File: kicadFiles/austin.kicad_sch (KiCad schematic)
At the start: 481 parts, among them J1 TYPE-C-31-M12_13, J5 ARM SWD, Q1 AO4406AL, Q2 DTC123J, SW1 MXSwitch, SW10 MXSwitch, SW100 MXSwitch, SW101 MXSwitch, SW102 MXSwitch, SW103 MXSwitch, SW104 MXSwitch, SW105 MXSwitch, SW106 MXSwitch, SW107 MXSwitch, SW108 MXSwitch, SW109 MXSwitch, SW11 MXSwitch, SW110 MXSwitch, SW111 MXSwitch, SW112 MXSwitch, SW113 MXSwitch, SW114 MXSwitch, SW12 MXSwitch, SW13 MXSwitch, SW14 MXSwitch, SW15 MXSwitch, SW16 MXSwitch, SW17 MXSwitch, SW18 MXSwitch, SW19 MXSwitch, SW2 MXSwitch, SW20 MXSwitch, SW21 MXSwitch, SW22 MXSwitch, SW23 MXSwitch, SW24 MXSwitch, SW25 MXSwitch, SW26 MXSwitch, SW27 MXSwitch, SW28 MXSwitch, SW29 MXSwitch, SW3 MXSwitch, SW30 MXSwitch, SW31 MXSwitch, SW32 MXSwitch, SW33 MXSwitch, SW34 MXSwitch, SW35 MXSwitch, SW36 MXSwitch, SW37 MXSwitch, SW38 MXSwitch, SW39 MXSwitch, SW4 MXSwitch, SW40 MXSwitch, SW41 MXSwitch, SW42 MXSwitch, SW43 MXSwitch, SW44 MXSwitch, SW45 MXSwitch, SW46 MXSwitch, SW47 MXSwitch, SW48 MXSwitch, SW49 MXSwitch, SW5 MXSwitch, SW50 MXSwitch, SW51 MXSwitch, SW52 MXSwitch, SW53 MXSwitch, SW54 MXSwitch, SW55 MXSwitch, SW56 MXSwitch, SW57 MXSwitch, SW58 ANSI LShift, SW59 MXSwitch, SW6 MXSwitch, SW60 MXSwitch, SW61 MXSwitch, SW62 MXSwitch, SW63 MXSwitch, SW64 MXSwitch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

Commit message: RGB placemente and routing, new MCU placement, rows traces patterns done
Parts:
- removed CB2, CB3, CB4: 100n, Capacitor_SMD:C_0805_2012Metric_Pad1.15x1.40mm_HandSolder, symbol Device:C_Small
- removed CB5: 10u, Capacitor_SMD:C_0805_2012Metric_Pad1.15x1.40mm_HandSolder, symbol Device:C_Small
- removed Q1: AO4406AL, acheronComponents:SOIC-8, symbol austin-rescue:AO4406AL-acheronSymbols-austin-rescue-austin-rescue
- removed RGP1: 10k, acheronComponents:R_SMD_1206, symbol Device:R_Small
- removed RGS1: 100, acheronComponents:R_SMD_1206, symbol Device:R_Small
- added C1, C11, C7: 1u, Capacitor_SMD:C_0805_2012Metric_Pad1.15x1.40mm_HandSolder, symbol Device:C_Small
- added C10, C5, C6: 100n, Capacitor_SMD:C_0805_2012Metric_Pad1.15x1.40mm_HandSolder, symbol Device:C_Small
- added C14, C15, C16, C17, C18, C19, C20, C21, C22, C23, C24, C25, C26, C27, C28, C29, C30, C31, C32, C33, C34, C35: 100n, Capacitor_SMD:C_0805_2012Metric, symbol Device:C
- added C8: 4.7u, Capacitor_SMD:C_0805_2012Metric_Pad1.15x1.40mm_HandSolder, symbol Device:C_Small
- added C9: 10n, Capacitor_SMD:C_0805_2012Metric_Pad1.15x1.40mm_HandSolder, symbol Device:C_Small
- added D109, D110, D111, D112, D113, D114, D115, D116, D117, D118, D119, D120, D121, D122, D123, D124, D125, D126, D127, D128: WS2812C, acheronComponents:LED_WS2812B_5.0x5.0mm_P3.2mm, symbol LED:WS2812B
- added Q1: AO3401A, Package_TO_SOT_SMD:SOT-23, symbol Transistor_FET:AO3401A
- added Q2: DTC123JKAT146, Package_TO_SOT_SMD:SOT-23, symbol acheronSymbols:DTC123J
- added R1: 1k, Resistor_SMD:R_0805_2012Metric, symbol Device:R
- added R119: 10k, Resistor_SMD:R_0805_2012Metric, symbol Device:R
- added R120, R121, R122, R123, R124, R125, R126, R127, R128, R129, R130, R131, R132, R133, R134, R135, R136, R137, R138, R139: 5R, Resistor_SMD:R_0805_2012Metric, symbol Device:R
- added R2: 100R, Resistor_SMD:R_0805_2012Metric, symbol Device:R
- added U4: TXS0101, acheronComponents:SOT-23-6, symbol acheronSymbols:TXS0101
- R10: renamed from RL8; value 360 -> 420; footprint acheronComponents:R_SMD_1206 -> Resistor_SMD:R_0805_2012Metric; Package (none) -> R0805
- R100: renamed from RL100; value 360 -> 420; footprint acheronComponents:R_SMD_1206 -> Resistor_SMD:R_0805_2012Metric; Package (none) -> R0805
- R101: renamed from RL101; value 360 -> 420; footprint acheronComponents:R_SMD_1206 -> Resistor_SMD:R_0805_2012Metric; Package (none) -> R0805
- R102: renamed from RL102; value 360 -> 420; footprint acheronComponents:R_SMD_1206 -> Resistor_SMD:R_0805_2012Metric; Package (none) -> R0805
- R103: renamed from RL103; value 360 -> 420; footprint acheronComponents:R_SMD_1206 -> Resistor_SMD:R_0805_2012Metric; Package (none) -> R0805
- R104: renamed from RL104; value 360 -> 420; footprint acheronComponents:R_SMD_1206 -> Resistor_SMD:R_0805_2012Metric; Package (none) -> R0805
- R105: renamed from RL105; value 360 -> 420; footprint acheronComponents:R_SMD_1206 -> Resistor_SMD:R_0805_2012Metric; Package (none) -> R0805
- R106: renamed from RL106; value 360 -> 420; footprint acheronComponents:R_SMD_1206 -> Resistor_SMD:R_0805_2012Metric; Package (none) -> R0805
- R107: renamed from RL107; value 360 -> 420; footprint acheronComponents:R_SMD_1206 -> Resistor_SMD:R_0805_2012Metric; Package (none) -> R0805
- R108: renamed from RL108; value 360 -> 420; footprint acheronComponents:R_SMD_1206 -> Resistor_SMD:R_0805_2012Metric; Package (none) -> R0805
- R11: renamed from RL9; value 360 -> 420; footprint acheronComponents:R_SMD_1206 -> Resistor_SMD:R_0805_2012Metric; Package (none) -> R0805
- R113: renamed from R7; value 360 -> 420
- R114: renamed from R8; value 360 -> 420
- R115: renamed from R9; value 360 -> 420
- R12: renamed from RL10; value 360 -> 420; footprint acheronComponents:R_SMD_1206 -> Resistor_SMD:R_0805_2012Metric; Package (none) -> R0805
- R13: renamed from RL11; value 360 -> 420; footprint acheronComponents:R_SMD_1206 -> Resistor_SMD:R_0805_2012Metric; Package (none) -> R0805
- R14: renamed from RL12; value 360 -> 420; footprint acheronComponents:R_SMD_1206 -> Resistor_SMD:R_0805_2012Metric; Package (none) -> R0805
- R15: renamed from RL13; value 360 -> 420; footprint acheronComponents:R_SMD_1206 -> Resistor_SMD:R_0805_2012Metric; Package (none) -> R0805
- R16: renamed from RL14; value 360 -> 420; footprint acheronComponents:R_SMD_1206 -> Resistor_SMD:R_0805_2012Metric; Package (none) -> R0805
- R17: renamed from RL15; value 360 -> 420; footprint acheronComponents:R_SMD_1206 -> Resistor_SMD:R_0805_2012Metric; Package (none) -> R0805
- R18: renamed from RL16; value 360 -> 420; footprint acheronComponents:R_SMD_1206 -> Resistor_SMD:R_0805_2012Metric; Package (none) -> R0805
- R19: renamed from RL17; value 360 -> 420; footprint acheronComponents:R_SMD_1206 -> Resistor_SMD:R_0805_2012Metric; Package (none) -> R0805
- R20: renamed from RL18; value 360 -> 420; footprint acheronComponents:R_SMD_1206 -> Resistor_SMD:R_0805_2012Metric; Package (none) -> R0805
- R21: renamed from RL19; value 360 -> 420; footprint acheronComponents:R_SMD_1206 -> Resistor_SMD:R_0805_2012Metric; Package (none) -> R0805
- R22: renamed from RL20; value 360 -> 420; footprint acheronComponents:R_SMD_1206 -> Resistor_SMD:R_0805_2012Metric; Package (none) -> R0805
- R23: renamed from RL21; value 360 -> 420; footprint acheronComponents:R_SMD_1206 -> Resistor_SMD:R_0805_2012Metric; Package (none) -> R0805
- R24: renamed from RL22; value 360 -> 420; footprint acheronComponents:R_SMD_1206 -> Resistor_SMD:R_0805_2012Metric; Package (none) -> R0805
- R25: renamed from RL23; value 360 -> 420; footprint acheronComponents:R_SMD_1206 -> Resistor_SMD:R_0805_2012Metric; Package (none) -> R0805
- R26: renamed from RL24; value 360 -> 420; footprint acheronComponents:R_SMD_1206 -> Resistor_SMD:R_0805_2012Metric; Package (none) -> R0805
- R27: renamed from RL25; value 360 -> 420; footprint acheronComponents:R_SMD_1206 -> Resistor_SMD:R_0805_2012Metric; Package (none) -> R0805
- R28: renamed from RL26; value 360 -> 420; footprint acheronComponents:R_SMD_1206 -> Resistor_SMD:R_0805_2012Metric; Package (none) -> R0805
- R29: renamed from RL27; value 360 -> 420; footprint acheronComponents:R_SMD_1206 -> Resistor_SMD:R_0805_2012Metric; Package (none) -> R0805
- R3: renamed from RL1; value 360 -> 420; footprint acheronComponents:R_SMD_1206 -> Resistor_SMD:R_0805_2012Metric; Package (none) -> R0805
- R30: renamed from RL28; value 360 -> 420; footprint acheronComponents:R_SMD_1206 -> Resistor_SMD:R_0805_2012Metric; Package (none) -> R0805
- R31: renamed from RL29; value 360 -> 420; footprint acheronComponents:R_SMD_1206 -> Resistor_SMD:R_0805_2012Metric; Package (none) -> R0805
- R32: renamed from RL30; value 360 -> 420; footprint acheronComponents:R_SMD_1206 -> Resistor_SMD:R_0805_2012Metric; Package (none) -> R0805
- R33: renamed from RL31; value 360 -> 420; footprint acheronComponents:R_SMD_1206 -> Resistor_SMD:R_0805_2012Metric; Package (none) -> R0805
- R34: renamed from RL32; value 360 -> 420; footprint acheronComponents:R_SMD_1206 -> Resistor_SMD:R_0805_2012Metric; Package (none) -> R0805
- R35: renamed from RL33; value 360 -> 420; footprint acheronComponents:R_SMD_1206 -> Resistor_SMD:R_0805_2012Metric; Package (none) -> R0805
- R36: renamed from RL34; value 360 -> 420; footprint acheronComponents:R_SMD_1206 -> Resistor_SMD:R_0805_2012Metric; Package (none) -> R0805
- R37: renamed from RL36; value 360 -> 420; footprint acheronComponents:R_SMD_1206 -> Resistor_SMD:R_0805_2012Metric; Package (none) -> R0805
- R38: renamed from RL37; value 360 -> 420; footprint acheronComponents:R_SMD_1206 -> Resistor_SMD:R_0805_2012Metric; Package (none) -> R0805
- R39: renamed from RL38; value 360 -> 420; footprint acheronComponents:R_SMD_1206 -> Resistor_SMD:R_0805_2012Metric; Package (none) -> R0805
- R4: renamed from RL2; value 360 -> 420; footprint acheronComponents:R_SMD_1206 -> Resistor_SMD:R_0805_2012Metric; Package (none) -> R0805
- R40: renamed from RL39; value 360 -> 420; footprint acheronComponents:R_SMD_1206 -> Resistor_SMD:R_0805_2012Metric; Package (none) -> R0805
- R41: renamed from RL40; value 360 -> 420; footprint acheronComponents:R_SMD_1206 -> Resistor_SMD:R_0805_2012Metric; Package (none) -> R0805
- R42: renamed from RL41; value 360 -> 420; footprint acheronComponents:R_SMD_1206 -> Resistor_SMD:R_0805_2012Metric; Package (none) -> R0805
- R43: renamed from RL42; value 360 -> 420; footprint acheronComponents:R_SMD_1206 -> Resistor_SMD:R_0805_2012Metric; Package (none) -> R0805
- R44: renamed from RL43; value 360 -> 420; footprint acheronComponents:R_SMD_1206 -> Resistor_SMD:R_0805_2012Metric; Package (none) -> R0805
- R45: renamed from RL44; value 360 -> 420; footprint acheronComponents:R_SMD_1206 -> Resistor_SMD:R_0805_2012Metric; Package (none) -> R0805
- R46: renamed from RL45; value 360 -> 420; footprint acheronComponents:R_SMD_1206 -> Resistor_SMD:R_0805_2012Metric; Package (none) -> R0805
- R47: renamed from RL46; value 360 -> 420; footprint acheronComponents:R_SMD_1206 -> Resistor_SMD:R_0805_2012Metric; Package (none) -> R0805
- R48: renamed from RL47; value 360 -> 420; footprint acheronComponents:R_SMD_1206 -> Resistor_SMD:R_0805_2012Metric; Package (none) -> R0805
- R49: renamed from RL48; value 360 -> 420; footprint acheronComponents:R_SMD_1206 -> Resistor_SMD:R_0805_2012Metric; Package (none) -> R0805
- R5: renamed from RL3; value 360 -> 420; footprint acheronComponents:R_SMD_1206 -> Resistor_SMD:R_0805_2012Metric; Package (none) -> R0805
- R50: renamed from RL49; value 360 -> 420; footprint acheronComponents:R_SMD_1206 -> Resistor_SMD:R_0805_2012Metric; Package (none) -> R0805
- R51: renamed from RL50; value 360 -> 420; footprint acheronComponents:R_SMD_1206 -> Resistor_SMD:R_0805_2012Metric; Package (none) -> R0805
- R52: renamed from RL51; value 360 -> 420; footprint acheronComponents:R_SMD_1206 -> Resistor_SMD:R_0805_2012Metric; Package (none) -> R0805
- R53: renamed from RL52; value 360 -> 420; footprint acheronComponents:R_SMD_1206 -> Resistor_SMD:R_0805_2012Metric; Package (none) -> R0805
- R54: renamed from RL53; value 360 -> 420; footprint acheronComponents:R_SMD_1206 -> Resistor_SMD:R_0805_2012Metric; Package (none) -> R0805
- R55: renamed from RL54; value 360 -> 420; footprint acheronComponents:R_SMD_1206 -> Resistor_SMD:R_0805_2012Metric; Package (none) -> R0805
- R56: renamed from RL55; value 360 -> 420; footprint acheronComponents:R_SMD_1206 -> Resistor_SMD:R_0805_2012Metric; Package (none) -> R0805
- R57: renamed from RL56; value 360 -> 420; footprint acheronComponents:R_SMD_1206 -> Resistor_SMD:R_0805_2012Metric; Package (none) -> R0805
- R58: renamed from RL57; value 360 -> 420; footprint acheronComponents:R_SMD_1206 -> Resistor_SMD:R_0805_2012Metric; Package (none) -> R0805
- R59: renamed from RL58; value 360 -> 420; footprint acheronComponents:R_SMD_1206 -> Resistor_SMD:R_0805_2012Metric; Package (none) -> R0805
- R6: renamed from RL4; value 360 -> 420; footprint acheronComponents:R_SMD_1206 -> Resistor_SMD:R_0805_2012Metric; Package (none) -> R0805
- R60: renamed from RL60; value 360 -> 420; footprint acheronComponents:R_SMD_1206 -> Resistor_SMD:R_0805_2012Metric; Package (none) -> R0805
- R61: renamed from RL62; value 360 -> 420; footprint acheronComponents:R_SMD_1206 -> Resistor_SMD:R_0805_2012Metric; Package (none) -> R0805
- R62: renamed from RL63; value 360 -> 420; footprint acheronComponents:R_SMD_1206 -> Resistor_SMD:R_0805_2012Metric; Package (none) -> R0805
- R63: renamed from RL64; value 360 -> 420; footprint acheronComponents:R_SMD_1206 -> Resistor_SMD:R_0805_2012Metric; Package (none) -> R0805
- R64: renamed from RL65; value 360 -> 420; footprint acheronComponents:R_SMD_1206 -> Resistor_SMD:R_0805_2012Metric; Package (none) -> R0805
- R65: renamed from RL66; value 360 -> 420; footprint acheronComponents:R_SMD_1206 -> Resistor_SMD:R_0805_2012Metric; Package (none) -> R0805
- R66: renamed from RL67; value 360 -> 420; footprint acheronComponents:R_SMD_1206 -> Resistor_SMD:R_0805_2012Metric; Package (none) -> R0805
- R67: renamed from RL68; value 360 -> 420; footprint acheronComponents:R_SMD_1206 -> Resistor_SMD:R_0805_2012Metric; Package (none) -> R0805
- R68: renamed from RL69; value 360 -> 420; footprint acheronComponents:R_SMD_1206 -> Resistor_SMD:R_0805_2012Metric; Package (none) -> R0805
- R69: renamed from RL70; value 360 -> 420; footprint acheronComponents:R_SMD_1206 -> Resistor_SMD:R_0805_2012Metric; Package (none) -> R0805
- R7: renamed from RL5; value 360 -> 420; footprint acheronComponents:R_SMD_1206 -> Resistor_SMD:R_0805_2012Metric; Package (none) -> R0805
- R70: renamed from RL71; value 360 -> 420; footprint acheronComponents:R_SMD_1206 -> Resistor_SMD:R_0805_2012Metric; Package (none) -> R0805
- R71: renamed from RL72; value 360 -> 420; footprint acheronComponents:R_SMD_1206 -> Resistor_SMD:R_0805_2012Metric; Package (none) -> R0805
- R72: renamed from RL73; value 360 -> 420; footprint acheronComponents:R_SMD_1206 -> Resistor_SMD:R_0805_2012Metric; Package (none) -> R0805
- R73: renamed from RL74; value 360 -> 420; footprint acheronComponents:R_SMD_1206 -> Resistor_SMD:R_0805_2012Metric; Package (none) -> R0805
- R74: renamed from RL75; value 360 -> 420; footprint acheronComponents:R_SMD_1206 -> Resistor_SMD:R_0805_2012Metric; Package (none) -> R0805
- R75: renamed from RL76; value 360 -> 420; footprint acheronComponents:R_SMD_1206 -> Resistor_SMD:R_0805_2012Metric; Package (none) -> R0805
- R76: renamed from RL77; value 360 -> 420; footprint acheronComponents:R_SMD_1206 -> Resistor_SMD:R_0805_2012Metric; Package (none) -> R0805
- R77: renamed from RL78; value 360 -> 420; footprint acheronComponents:R_SMD_1206 -> Resistor_SMD:R_0805_2012Metric; Package (none) -> R0805
- R78: renamed from RL79; value 360 -> 420; footprint acheronComponents:R_SMD_1206 -> Resistor_SMD:R_0805_2012Metric; Package (none) -> R0805
- R79: renamed from RL80; value 360 -> 420; footprint acheronComponents:R_SMD_1206 -> Resistor_SMD:R_0805_2012Metric; Package (none) -> R0805
- R8: renamed from RL6; value 360 -> 420; footprint acheronComponents:R_SMD_1206 -> Resistor_SMD:R_0805_2012Metric; Package (none) -> R0805
- R80: renamed from RL81; value 360 -> 420; footprint acheronComponents:R_SMD_1206 -> Resistor_SMD:R_0805_2012Metric; Package (none) -> R0805
- R81: renamed from RL82; value 360 -> 420; footprint acheronComponents:R_SMD_1206 -> Resistor_SMD:R_0805_2012Metric; Package (none) -> R0805
- R82: renamed from RL83; value 360 -> 420; footprint acheronComponents:R_SMD_1206 -> Resistor_SMD:R_0805_2012Metric; Package (none) -> R0805
- R83: renamed from RL84; value 360 -> 420; footprint acheronComponents:R_SMD_1206 -> Resistor_SMD:R_0805_2012Metric; Package (none) -> R0805
- R84: renamed from RL85; value 360 -> 420; footprint acheronComponents:R_SMD_1206 -> Resistor_SMD:R_0805_2012Metric; Package (none) -> R0805
- R85: renamed from RL86; value 360 -> 420; footprint acheronComponents:R_SMD_1206 -> Resistor_SMD:R_0805_2012Metric; Package (none) -> R0805
- R86: renamed from RL87; value 360 -> 420; footprint acheronComponents:R_SMD_1206 -> Resistor_SMD:R_0805_2012Metric; Package (none) -> R0805
- R87: renamed from RL88; value 360 -> 420; footprint acheronComponents:R_SMD_1206 -> Resistor_SMD:R_0805_2012Metric; Package (none) -> R0805
- R88: renamed from RL89; value 360 -> 420; footprint acheronComponents:R_SMD_1206 -> Resistor_SMD:R_0805_2012Metric; Package (none) -> R0805
- R89: renamed from RL90; value 360 -> 420; footprint acheronComponents:R_SMD_1206 -> Resistor_SMD:R_0805_2012Metric; Package (none) -> R0805
- R9: renamed from RL7; value 360 -> 420; footprint acheronComponents:R_SMD_1206 -> Resistor_SMD:R_0805_2012Metric; Package (none) -> R0805
- R90: renamed from RL91; value 360 -> 420; footprint acheronComponents:R_SMD_1206 -> Resistor_SMD:R_0805_2012Metric; Package (none) -> R0805
- R91: renamed from RL35; value 360 -> 420; footprint acheronComponents:R_SMD_1206 -> Resistor_SMD:R_0805_2012Metric; Package (none) -> R0805
- R92: renamed from RL92; value 360 -> 420; footprint acheronComponents:R_SMD_1206 -> Resistor_SMD:R_0805_2012Metric; Package (none) -> R0805
- R93: renamed from RL93; value 360 -> 420; footprint acheronComponents:R_SMD_1206 -> Resistor_SMD:R_0805_2012Metric; Package (none) -> R0805
- R94: renamed from RL94; value 360 -> 420; footprint acheronComponents:R_SMD_1206 -> Resistor_SMD:R_0805_2012Metric; Package (none) -> R0805
- R95: renamed from RL95; value 360 -> 420; footprint acheronComponents:R_SMD_1206 -> Resistor_SMD:R_0805_2012Metric; Package (none) -> R0805
- R96: renamed from RL96; value 360 -> 420; footprint acheronComponents:R_SMD_1206 -> Resistor_SMD:R_0805_2012Metric; Package (none) -> R0805
- R97: renamed from RL97; value 360 -> 420; footprint acheronComponents:R_SMD_1206 -> Resistor_SMD:R_0805_2012Metric; Package (none) -> R0805
- R98: renamed from RL98; value 360 -> 420; footprint acheronComponents:R_SMD_1206 -> Resistor_SMD:R_0805_2012Metric; Package (none) -> R0805
- R99: renamed from RL99; value 360 -> 420; footprint acheronComponents:R_SMD_1206 -> Resistor_SMD:R_0805_2012Metric; Package (none) -> R0805
- U2: renamed from U1; value STM32F072_LQFP48 -> STM32F072CBT6; symbol austin-rescue:STM32F072_LQFP48-acheronSymbols-austin-rescue-austin-rescue -> acheronSymbols:STM32F072-LQFP48; LCSC Part Number (none) -> C81720; Manufacturer (none) -> STMicroelectronics; Manufacturer Part Number (none) -> STM32F072CBT6; Package (none) -> LQFP-48
- renumbered C3 to C12, C4 to C13, CB1 to C2, C1 to C3, C2 to C4, D103 to D100, D105 to D101, D106 to D102, D107 to D103, D108 to D104, D104 to D105, D58 to D106, D78 to D107, D60 to D108, D35 to D34, D36 to D35, D37 to D36, D38 to D37, D39 to D38, D40 to D39, D41 to D40, D42 to D41, D43 to D42, D44 to D43, D45 to D44, D46 to D45, D47 to D46, D48 to D47, D49 to D48, D50 to D49, D51 to D50, D52 to D51, D53 to D52, D54 to D53, D55 to D54, D56 to D55, D57 to D56, D61 to D57, D62 to D58, D63 to D59, D64 to D60, D65 to D61, D66 to D62, D67 to D63, D68 to D64, D69 to D65, D70 to D66, D71 to D67, D72 to D68, D73 to D69, D74 to D70, D75 to D71, D76 to D72, D77 to D73, D59 to D74, D90 to D75, D79 to D76, D34 to D77, D80 to D78, D81 to D79, D82 to D80, D83 to D81, D84 to D82, D85 to D83, D86 to D84, D87 to D85, D88 to D86, D89 to D87, D91 to D88, D92 to D89, D93 to D90, D94 to D91, D95 to D92, D96 to D93, D97 to D94, D98 to D95, D99 to D96, D100 to D97, D101 to D98, D102 to D99, J5 to J1, J1 to J2, LED109 to LED100, LED110 to LED101, LED97 to LED102, LED98 to LED103, LED99 to LED104, LED111 to LED105, LED100 to LED106, LED101 to LED107, LED102 to LED108, LED103 to LED109, LED104 to LED110, LED112 to LED111, LED105 to LED112, LED106 to LED113, LED107 to LED114, LED108 to LED115, LED35 to LED34, LED34 to LED35, LED114 to LED54, LED54 to LED55, LED55 to LED56, LED56 to LED57, LED57 to LED58, LED58 to LED59, LED61 to LED60, LED60 to LED61, LED115 to LED73, LED73 to LED74, LED74 to LED75, LED75 to LED76, LED76 to LED77, LED77 to LED78, LED78 to LED79, LED59 to LED80, LED79 to LED81, LED80 to LED82, LED81 to LED83, LED82 to LED84, LED83 to LED85, LED84 to LED86, LED85 to LED87, LED86 to LED88, LED87 to LED89, LED88 to LED90, LED89 to LED91, LED90 to LED92, LED91 to LED93, LED96 to LED94, LED92 to LED95, LED93 to LED96, LED94 to LED97, LED95 to LED98, LED113 to LED99, LEDSCRL1 to LEDSCR1, Q2 to Q3, R1 to R109, R10 to R110, R2 to R111, R3 to R112, R4 to R116, R5 to R117, R6 to R118, SW99 to SW100, SW100 to SW101, SW101 to SW102, SW102 to SW103, SW103 to SW104, SW98 to SW111, SW111 to SW112, SW104 to SW113, SW112 to SW114, SW35 to SW34, SW36 to SW35, SW37 to SW36, SW38 to SW37, SW39 to SW38, SW34 to SW39, SW113 to SW40, SW40 to SW41, SW41 to SW42, SW42 to SW43, SW43 to SW44, SW44 to SW45, SW45 to SW46, SW46 to SW47, SW47 to SW48, SW48 to SW49, SW49 to SW50, SW50 to SW51, SW51 to SW52, SW52 to SW53, SW53 to SW54, SW54 to SW55, SW55 to SW56, SW56 to SW57, SW57 to SW58, SW114 to SW59, SW62 to SW61, SW63 to SW62, SW64 to SW63, SW65 to SW64, SW66 to SW65, SW67 to SW66, SW68 to SW67, SW69 to SW68, SW70 to SW69, SW71 to SW70, SW72 to SW71, SW73 to SW72, SW74 to SW73, SW75 to SW74, SW76 to SW75, SW77 to SW76, SW59 to SW77, SW61 to SW78, SW58 to SW79, SW90 to SW80, SW79 to SW81, SW78 to SW82, SW80 to SW83, SW81 to SW84, SW82 to SW85, SW83 to SW86, SW84 to SW87, SW85 to SW88, SW86 to SW89, SW87 to SW90, SW88 to SW91, SW89 to SW92, SW91 to SW93, SW92 to SW94, SW93 to SW95, SW94 to SW96, SW95 to SW97, SW96 to SW98, SW97 to SW99, U2 to U1
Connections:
- net 3.3V: now also C2.2, C1.2, C10.2, C11.2, C5.1, C6.2, C7.2, C8.2, C9.2; no longer C2.1
- net 5V: now also C15.1, Q1.2 (S), R1.1, R120.2, R121.2, R122.2, R123.2, R124.2, R125.2, R126.2, R127.2, R128.2, R129.2, R130.2, R131.2, R132.2, R133.2, R134.2, R135.2, R136.2, R137.2, R138.2, R139.2, U4.6 (VCCB); no longer R10.1, R100.1, R101.1, R102.1, R103.1, R104.1, R105.1, R106.1, R107.1, R108.1, R11.1, R12.1, R13.1, R14.1, R15.1, R16.1, R17.1, R18.1, R19.1, R20.1, R21.1, R22.1, R23.1, R24.1, R25.1, R26.1, R27.1, R28.1, R29.1, R3.1, R30.1, R31.1, R32.1, R33.1, R34.1, R35.1, R36.1, R37.1, R38.1, R39.1, R4.1, R40.1, R41.1, R42.1, R43.1, R44.1, R45.1, R46.1, R47.1, R48.1, R49.1, R5.1, R50.1, R51.1, R52.1, R53.1, R54.1, R55.1, R56.1, R57.1, R58.1, R59.1, R6.1, R60.1, R61.1, R62.1, R63.1, R64.1, R65.1, R66.1, R67.1, R68.1, R69.1, R7.1, R70.1, R71.1, R72.1, R73.1, R74.1, R75.1, R76.1, R77.1, R78.1, R79.1, R8.1, R80.1, R81.1, R82.1, R83.1, R84.1, R85.1, R86.1, R87.1, R88.1, R89.1, R9.1, R90.1, R91.1, R92.1, R93.1, R94.1, R95.1, R96.1, R97.1, R98.1, R99.1
- net Col1: now also SW1.2 (Row); no longer SW1.1 (Col), U2.21 (SPI2_CK/I2C2_SCL/TIM2_CH3/PB10)
- net Col10: now also SW10.2 (Row); no longer SW10.1 (Col), U2.15 (SPI1_SCK/I2S1_CK/ADCIN4/DACOUT1/PA5)
- net Col11: no longer U2.38 (PA15)
- net Col12: no longer U2.39 (SPI1_SCK/I2S1CK/PB3)
- net Col13: no longer U2.40 (SPI1_MISO_I2S1MCK/PB4)
- net Col14: no longer U2.41 (TIM3_CH2/SPI1_MOSI/I2S1_SD/I2C1_SMBA/PB5)
- net Col15: no longer U2.45 (I2C1SCL/PB8)
- net Col16: no longer U2.13 (TIM2_CH4/ADCIN3/PA3)
- net Col17: no longer U2.4 (PC15/Osc32Out)
- net Col18: no longer U2.3 (PC14/Osc32In)
- net Col19: no longer U2.6 (PF1/OscOut)
- net Col2: no longer U2.22 (I2C2_SDA/TIM2_CH4/EVENTOUT/PB11)
- net Col3: no longer U2.25 (EVENTOUT/PB12)
- net Col4: no longer U2.26 (SPI2_SCK/I2S2_CK/I2C2_SCL/PB13)
- net Col5: no longer U2.27 (SPI2_MISO/I2S2_MCK/I2C2_SDA/PB14)
- net Col6: now also SW6.2 (Row); no longer SW6.1 (Col), U2.28 (SPI2_MOSI/I2S2_SD/PB15)
- net Col7: no longer U2.29 (TIM1_CH1/EVENTOUT/MCO/PA8)
- net Col8: no longer U2.30 (TIM1_CH2/PA9)
- net Col9: no longer U2.31 (TIM1_CH3/PA10)
- net GND: now also C2.1, C1.1, C10.1, C11.1, C14.1, C15.2, C16.1, C17.1, C18.1, C19.1, C20.1, C21.1, C22.1, C23.1, C24.1, C25.1, C26.1, C27.1, C28.1, C29.1, C30.1, C31.1, C32.1, C33.1, C34.1, C35.1, C5.2, C6.1, C7.1, C8.1, C9.1, D109.3 (VSS), D110.3 (VSS), D111.3 (VSS), D112.3 (VSS), D113.3 (VSS), D114.3 (VSS), D115.3 (VSS), D116.3 (VSS), D117.3 (VSS), D118.3 (VSS), D119.3 (VSS), D120.3 (VSS), D121.3 (VSS), D122.3 (VSS), D123.3 (VSS), D124.3 (VSS), D125.3 (VSS), D126.3 (VSS), D127.3 (VSS), D128.3 (VSS), Q2.2 (E), U4.2 (GND); no longer C2.2
- net INDICATOR1: no longer U2.10 (ADCIN2/PA0)
- net INDICATOR2: no longer U2.12 (TIM2_CH3/ADCIN2/WKUP4/PA2)
- net INDICATOR3: no longer U2.11 (ADCIN1/PA1)
- net LED_PWM: now also Q2.1 (B)
- net Row1: no longer U2.2 (PC13/WKUP2)
- net Row2: no longer U2.14 (SPI1_NSS/I2S1_WS/ADCIN4/DACOUT2/PA4)
- net Row3: no longer U2.17 (SPI1_MOSI/I2S1_SD/TIM3_CH2/ADCIN7/PA7)
- net Row4: no longer U2.18 (TIM3_CH3/ADCIN8/PB0)
- net Row5: no longer U2.19 (TIM3_CH4/ADCIN9/PB1)
- net Row6: no longer U2.20 (PB2)
- net at D1.2 (A): now also SW1.1 (Col); no longer SW1.2 (Row)
- net at D6.2 (A): now also SW6.1 (Col); no longer SW6.2 (Row)
- net at D10.2 (A): now also SW10.1 (Col); no longer SW10.2 (Row)
- new net: Q1.3 (D), R10.1, R100.1, R101.1, R102.1, R103.1, R104.1, R105.1, R106.1, R107.1, R108.1, R11.1, R12.1, R13.1, R14.1, R15.1, R16.1, R17.1, R18.1, R19.1, R20.1, R21.1, R22.1, R23.1, R24.1, R25.1, R26.1, R27.1, R28.1, R29.1, R3.1, R30.1, R31.1, R32.1, R33.1, R34.1, R35.1, R36.1, R37.1, R38.1, R39.1, R4.1, R40.1, R41.1, R42.1, R43.1, R44.1, R45.1, R46.1, R47.1, R48.1, R49.1, R5.1, R50.1, R51.1, R52.1, R53.1, R54.1, R55.1, R56.1, R57.1, R58.1, R59.1, R6.1, R60.1, R61.1, R62.1, R63.1, R64.1, R65.1, R66.1, R67.1, R68.1, R69.1, R7.1, R70.1, R71.1, R72.1, R73.1, R74.1, R75.1, R76.1, R77.1, R78.1, R79.1, R8.1, R80.1, R81.1, R82.1, R83.1, R84.1, R85.1, R86.1, R87.1, R88.1, R89.1, R9.1, R90.1, R91.1, R92.1, R93.1, R94.1, R95.1, R96.1, R97.1, R98.1, R99.1
- new net: C33.2, D126.1 (VDD), R137.1
- new net: D126.2 (DOUT), D127.4 (DIN)
- new net: D125.2 (DOUT), D126.4 (DIN)
- new net: C28.2, D121.1 (VDD), R132.1
- new net: C23.2, D116.1 (VDD), R127.1
- new net: C27.2, D120.1 (VDD), R131.1
- new net: R119.1, U4.5 (OE)
- new net: C26.2, D119.1 (VDD), R130.1
- new net: C16.2, D109.1 (VDD), R120.1
- new net: C31.2, D124.1 (VDD), R135.1
- new net: C22.2, D115.1 (VDD), R126.1
- new net: Q2.3 (C), R1.2, R2.2
- new net: D116.2 (DOUT), D117.4 (DIN)
- new net: D115.2 (DOUT), D116.4 (DIN)
- new net: Q1.1 (G), R2.1
- new net: C32.2, D125.1 (VDD), R136.1
- new net: D124.2 (DOUT), D125.4 (DIN)
- new net: D119.2 (DOUT), D120.4 (DIN)
- new net: D118.2 (DOUT), D119.4 (DIN)
- new net: C24.2, D117.1 (VDD), R128.1
- new net: C19.2, D112.1 (VDD), R123.1
- new net: D114.2 (DOUT), D115.4 (DIN)
- new net: C25.2, D118.1 (VDD), R129.1
- new net: C29.2, D122.1 (VDD), R133.1
- new net: D121.2 (DOUT), D122.4 (DIN)
- new net: D120.2 (DOUT), D121.4 (DIN)
- new net: C21.2, D114.1 (VDD), R125.1
- new net: D113.2 (DOUT), D114.4 (DIN)
- new net: C30.2, D123.1 (VDD), R134.1
- new net: D123.2 (DOUT), D124.4 (DIN)
- new net: D122.2 (DOUT), D123.4 (DIN)
- new net: D109.2 (DOUT), D110.4 (DIN)
- new net: C35.2, D128.1 (VDD), R139.1
- new net: C20.2, D113.1 (VDD), R124.1
- new net: D117.2 (DOUT), D118.4 (DIN)
- new net: C17.2, D110.1 (VDD), R121.1
- new net: D110.2 (DOUT), D111.4 (DIN)
- new net: D112.2 (DOUT), D113.4 (DIN)
- new net: D111.2 (DOUT), D112.4 (DIN)
- new net: C34.2, D127.1 (VDD), R138.1
- new net: D127.2 (DOUT), D128.4 (DIN)
- new net: C18.2, D111.1 (VDD), R122.1
- new net 3V3: C14.2, R119.2, U4.1 (VCCA)
- new net RGB_3V3: U2.28 (SPI2_MOSI/I2S2_SD/PB15), U4.3 (A)
- new net RGB_5V: D109.4 (DIN), U4.4 (B)
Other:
- note removed: "Bypass capacitors"
- note removed: "CBs for "Capacitors - Bypass""
- note removed: "CRI for Capacitor - Regulator Input"
- note removed: "CRO for Capacitor - Regulator Output"
- note removed: "DF for "Diode - Fuse""
- note removed: "DS33 for "Schottky Diode - 3.3V""
- note removed: "RGP for "Gate Parallel" RGS for "Gate Series""
- moved on the sheet: C2, LED1, LED10, LED100, LED101, LED102, LED103, LED104, LED105, LED106, LED107, LED108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

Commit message: 3rd and 4th rows routing, hybrid dual package footprint for MCU
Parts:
- added R140: 420, Resistor_SMD:R_0805_2012Metric, symbol Device:R_Small
- U2: footprint acheronComponents:LQFP-48_7x7mm_P0.5mm -> acheronComponents:LQFP48_UFQFPN48_7x7mm_P0.5mm; symbol acheronSymbols:STM32F072-LQFP48 -> acheronSymbols:STM32F072-UFQFPN48; Manufacturer Part Number STM32F072CBT6 -> STM32F072CBU6; Package LQFP-48 -> UFQFPN-48
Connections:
- net 5V: now also LEDCAPS1.A, LEDNUM1.A, LEDSCR1.A
- net Col1: now also SW20.2 (Row); no longer SW20.1 (Col)
- net Col10: no longer SW101.1 (Col)
- net Col11: now also SW101.1 (Col); no longer SW102.1 (Col)
- net Col12: now also SW102.1 (Col); no longer SW103.1 (Col)
- net Col13: no longer SW104.1 (Col)
- net Col14: now also SW104.1 (Col), SW73.1 (Col)
- net Col15: now also SW74.1 (Col), SW94.1 (Col); no longer SW73.1 (Col)
- net Col16: now also SW75.1 (Col), SW95.1 (Col); no longer SW74.1 (Col), SW94.1 (Col)
- net Col17: now also SW76.1 (Col), SW96.1 (Col); no longer SW75.1 (Col), SW95.1 (Col)
- net Col18: now also SW77.1 (Col), SW97.1 (Col); no longer SW76.1 (Col), SW96.1 (Col)
- net Col19: no longer SW77.1 (Col), SW97.1 (Col)
- net Col2: now also SW42.2 (Row); no longer SW42.1 (Col)
- net GND: now also U2.49 (PAD); no longer LEDCAPS1.K, LEDNUM1.K, LEDSCR1.K
- net INDICATOR1: now also R113.2; no longer R113.1
- net Row3: now also D104.1 (K)
- net Row6: no longer D104.1 (K)
- net at Q1.3 (D), R10.1, R100.1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: now also R140.1
- net at D20.2 (A): now also SW20.1 (Col); no longer SW20.2 (Row)
- net at D40.2 (A): now also SW42.1 (Col); no longer SW42.2 (Row)
- net at LED72.A, R71.2: no longer LED73.A
- net at R114.2: now also LEDNUM1.K; no longer LEDNUM1.A
- net at R115.2: now also LEDCAPS1.K; no longer LEDCAPS1.A
- new net: LEDSCR1.K, R113.1
- new net: LED73.A, R140.2
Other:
- note added: "GRAVE"
- note removed: "`~"
- moved on the sheet: D100, D104, D70, D71, D72, D73, D74, D89, D90, D91, D92, D97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

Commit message: Routing finished. DRC and label pending
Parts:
- added J3: Conn_01x04, acheronConnectors:PinHeader_1x4_P2.54mm_Vertical, symbol Connector_Generic:Conn_01x04
- C1, C10, C11, C2, C5, C6, C7, C8: footprint Capacitor_SMD:C_0805_2012Metric_Pad1.15x1.40mm_HandSolder -> Capacitor_SMD:C_0402_1005Metric; Package (none) -> C0402
- C12, C13: footprint Capacitor_SMD:C_0805_2012Metric_Pad1.15x1.40mm_HandSolder -> Capacitor_SMD:C_0805_2012Metric
- C9: footprint Capacitor_SMD:C_0805_2012Metric_Pad1.15x1.40mm_HandSolder -> Capacitor_SMD:C_0402_1005Metric
- J1: footprint acheronConnectors:Conn_ARM_JTAG_SWD_6 -> acheronConnectors:Conn_ARM_JTAG_SWD_8; symbol Connector_Generic:Conn_02x03_Odd_Even -> Connector_Generic:Conn_02x04_Odd_Even
- R116, R117, R118: footprint acheronComponents:R_SMD_1206 -> Resistor_SMD:R_0805_2012Metric
- U2: LCSC Part Number C81720 -> C92504; Package UFQFPN-48 -> UFQFPN48
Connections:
- net 3.3V is gone; now on net 3V3: C1.2, C10.2, C11.2, C2.2, C4.1, C5.1, C6.2, C7.2, C8.2, C9.2, D106.2 (A), J1.1 (Pin_1), R110.1, S1.1, U1.2 (VO), U2.1 (VBAT), U2.24 (VDD), U2.36 (VDDIO2), U2.48 (VDD), U2.9 (VDDA)
- net nRST is gone; now on net NRST: J1.3 (Pin_3)
- net 3V3: now also J3.1 (Pin_1)
- net BOOT0: now also J1.8 (Pin_8)
- net Col1: now also U2.22 (PB11/TIM2_CH4/I2C2_SDA)
- net Col10: now also U2.4 (PC15/OSC32_OUT)
- net Col11: now also U2.3 (PC14/OSC32_IN)
- net Col12: now also U2.2 (PC13)
- net Col13: now also U2.21 (PB10/SPI2_SCK/I2C2_SCL/TIM2_CH3)
- net Col14: now also U2.20 (PB2)
- net Col15: now also U2.42 (I2C1_SCL/PB6)
- net Col16: now also U2.41 (SPI1_MOSI/I2S1_SD/TIM3_CH2/PB5)
- net Col17: now also U2.40 (SPI1_MISO/I2S1_MCK/TIM3_CH1/PB4)
- net Col18: now also U2.39 (SPI1_SCK/I2S1_CK/TIM2_CH2/PB3)
- net Col19: now also U2.38 (PA15)
- net Col2: now also U2.15 (PA5/ADC_IN5/DAC_OUT2)
- net Col3: now also U2.14 (PA4/TIM14_CH1/ADC_IN4)
- net Col4: now also U2.13 (PA3/TIM15_CH2/ADC_IN3)
- net Col5: now also U2.12 (PA2/ADC_IN2)
- net Col6: now also U2.11 (PA1/ADC_IN1)
- net Col7: now also U2.10 (PA0/ADC_IN0)
- net Col8: now also U2.6 (PF1/OSC_OUT)
- net Col9: now also U2.5 (PF0/OSC_IN)
- net GND: now also J1.7 (Pin_7), J3.4 (Pin_4)
- net INDICATOR1: now also U2.19 (PB1/TIM3_CH4/TIM14_CH1/ADC_IN9)
- net INDICATOR2: now also U2.17 (PA7/TIM3_CH2/TIM14_CH1/ADC_IN7)
- net INDICATOR3: now also U2.18 (PB0/TIM3_CH3/ADC_IN8)
- net Row1: now also U2.46 (SPI2_NSS/I2S2_WS/I2C1_SDA/TIM17_CH1/PB9)
- net Row2: now also U2.45 (I2C1_SCL/TIM16_CH1/PB8)
- net Row3: now also U2.43 (2C1_SDA/PB7)
- net Row4: now also U2.25 (PB12)
- net Row5: now also U2.27 (SPI2_MISO/I2S2_MCK/I2C2_SDA/TIM15_CH1/PB14)
- net Row6: now also U2.29 (TIM1_CH1/PA8)
- net EXTRA2: now reaches U2.30 (TIM1_CH2/PA9)
- net EXTRA2: now also J3.3 (Pin_3)
- net EXTRA1: now reaches U2.31 (TIM1_CH3/PA10)
- net EXTRA1: now also J3.2 (Pin_2)
- no-connect marks 2 -> 3

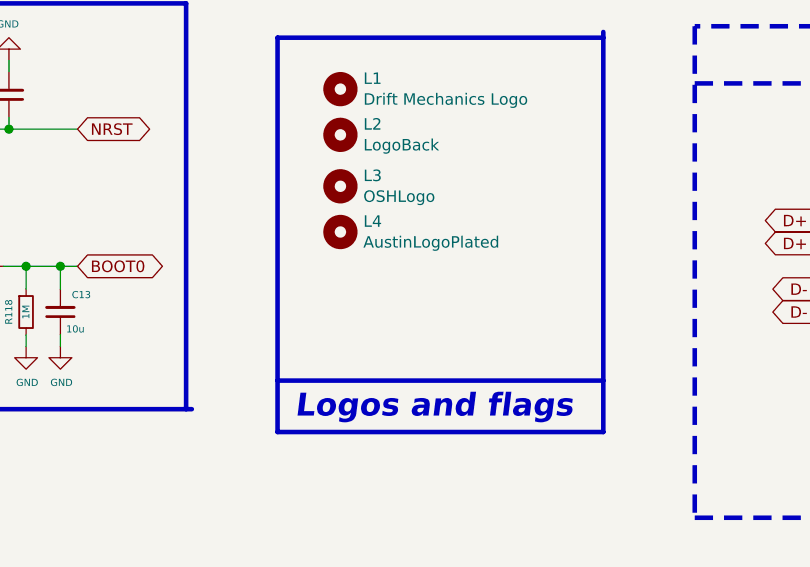
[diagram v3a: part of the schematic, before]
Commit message: Updated label, finish fab layers
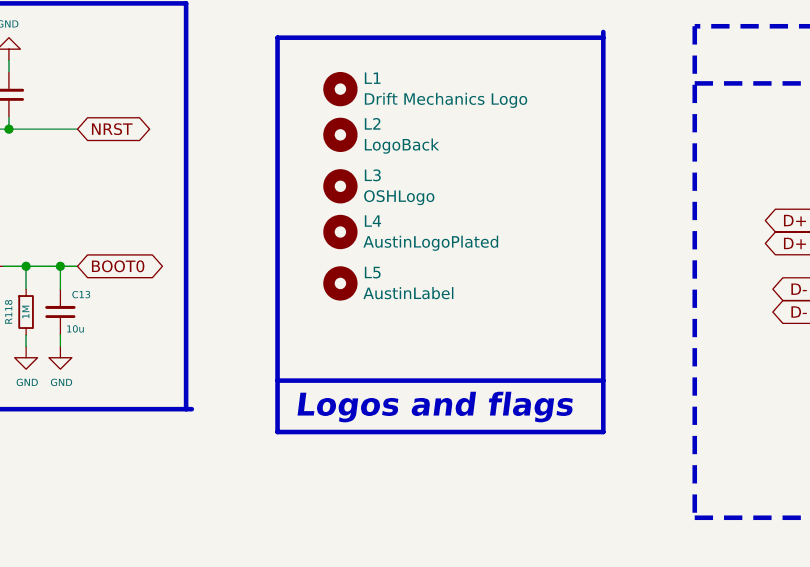
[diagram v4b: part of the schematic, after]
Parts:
- added L5: AustinLabel, austinLogo:austinLabel, symbol Mechanical:MountingHole
- L1, L2, L3, L4: now left out of the parts list
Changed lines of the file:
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@@
   (title_block
     (title "AustinPCB")
-    (date "2020-11-02")
-    (rev "v2.0.4")
+    (date "2020-11-03")
+    (rev "v2.0.5")
     (company "Designed by Gondolindrim")
     (comment 1 "In partnership with driftingbunnies and PheonixStar")
@@
   (junction (at 1123.95 515.62) (diameter 1.016) (color 0 0 0 0))
   (no_connect (at 234.315 304.165))
-  (no_connect (at 234.315 301.625))
   (no_connect (at 730.25 319.405))
+  (no_connect (at 234.315 301.625))
   (wire (pts (xy 44.45 35.56) (xy 66.04 35.56))
     (stroke (width 0) (type solid) (color 0 0 0 0))
@@
   )
   (symbol (lib_id "Mechanical:MountingHole") (at 266.7 364.49 0) (unit 1)
-    (in_bom yes) (on_board yes)
+    (in_bom no) (on_board yes)
     (property "Reference" "L1" (id 0) (at 269.24 363.3216 0)
       (effects (font (size 1.27 1.27)) (justify left))
@@
   )
   (symbol (lib_id "Mechanical:MountingHole") (at 266.7 369.57 0) (unit 1)
-    (in_bom yes) (on_board yes)
+    (in_bom no) (on_board yes)
     (property "Reference" "L2" (id 0) (at 269.24 368.4016 0)
       (effects (font (size 1.27 1.27)) (justify left))
@@
   )
   (symbol (lib_name "Mechanical:MountingHole_1") (lib_id "Mechanical:MountingHole") (at 266.7 375.285 0) (unit 1)
-    (in_bom yes) (on_board yes)
+    (in_bom no) (on_board yes)
     (property "Reference" "L3" (id 0) (at 269.24 374.1166 0)
       (effects (font (size 1.27 1.27)) (justify left))
@@
   )
   (symbol (lib_id "Mechanical:MountingHole") (at 266.7 380.365 0) (unit 1)
-    (in_bom yes) (on_board yes)
+    (in_bom no) (on_board yes)
     (property "Reference" "L4" (id 0) (at 269.24 379.1966 0)
       (effects (font (size 1.27 1.27)) (justify left))
@@
     )
   )
+  (symbol (lib_id "Mechanical:MountingHole") (at 266.7 386.08 0) (unit 1)
+    (in_bom no) (on_board yes)
+    (property "Reference" "L5" (id 0) (at 269.24 384.9116 0)
+      (effects (font (size 1.27 1.27)) (justify left))
+    )
+    (property "Value" "AustinLabel" (id 1) (at 269.24 387.223 0)
+      (effects (font (size 1.27 1.27)) (justify left))
+    )
+    (property "Footprint" "austinLogo:austinLabel" (id 2) (at 266.7 386.08 0)
+      (effects (font (size 1.27 1.27)) hide)
+    )
+    (property "Datasheet" "~" (id 3) (at 266.7 386.08 0)
+      (effects (font (size 1.27 1.27)) hide)
+    )
+  )
   (symbol (lib_id "Device:CP_Small") (at 423.545 252.095 0) (unit 1)
     (in_bom yes) (on_board yes)
@@
       (reference "L4") (unit 1) (value "AustinLogoPlated") (footprint "austinLogo:austinLogo_16x40_Plated")
     )
+    (path "/6dd2211e-f77c-4e38-904a-26c891874e38"
+      (reference "L5") (unit 1) (value "AustinLabel") (footprint "austinLogo:austinLabel")
+    )
     (path "/00000000-0000-0000-0000-00005d1ebf5b"

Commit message: Update fuse metadata, DRC ran, organized schematic
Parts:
- F1: value 1.5A trip polyfuse -> miniSMDC110F; footprint Fuse:Fuse_1812_4532Metric_Pad1.30x3.40mm_HandSolder -> acheronComponents:Fuse_1812_4532; LCSC Part Number (none) -> C207188; Manufacturer (none) -> Littelfuse; Manufacturer Part Number (none) -> miniSMDC110F; Package (none) -> F1812
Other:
- note added: "RGB"
- note added: "USB ESD"
- note removed: "USD ESD"
- moved on the sheet: C1, C10, C11, C12, C13, C14, C15, C16, C17, C18, C19, C2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
